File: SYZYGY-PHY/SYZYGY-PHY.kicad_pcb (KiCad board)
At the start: 4 copper layers, 57.7 x 27 mm, 45 parts, among them J1 QTH-020-01-X-D-DP-A, J2 ARJM11C7-502-KB-EW2, J3 Conn_01x10, U1 GPY111, U2 TXB0106RGY, U3 TXB0106RGY, Y1 Crystal_GND24

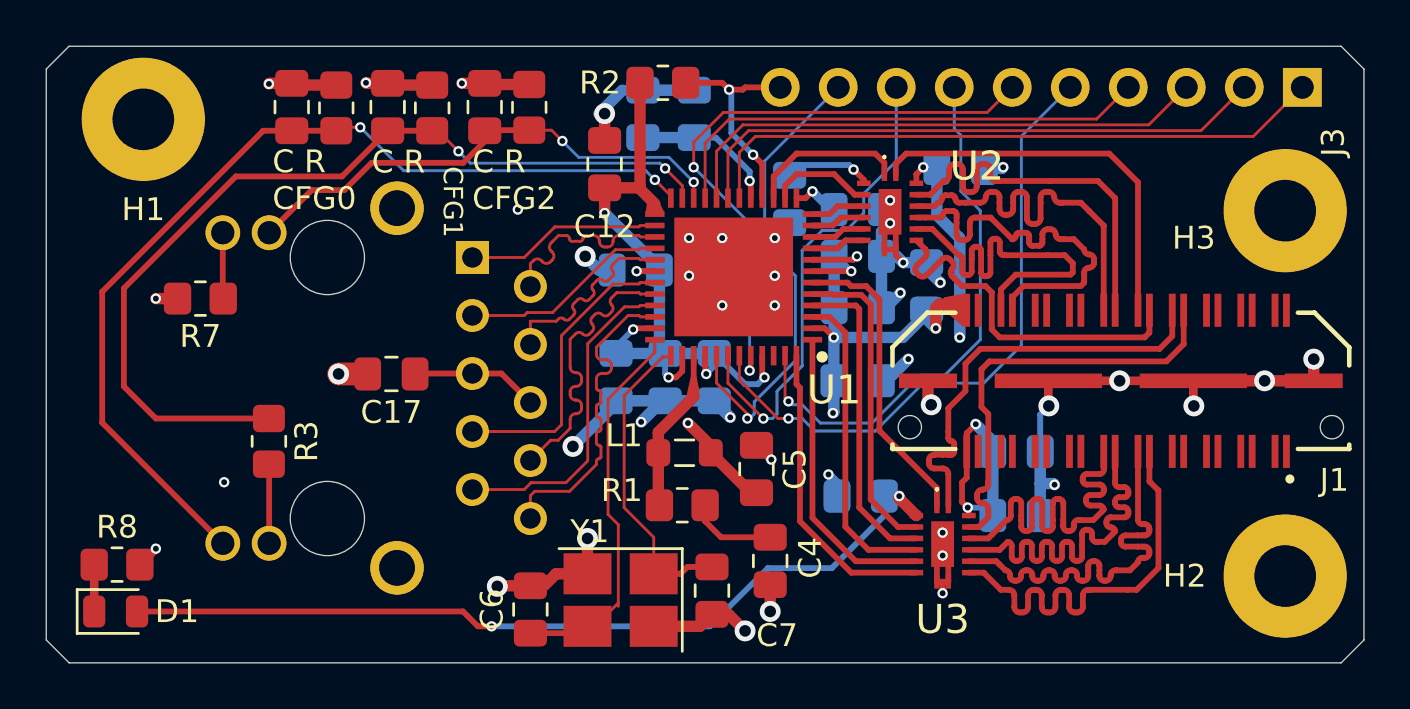
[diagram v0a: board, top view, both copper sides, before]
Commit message: misc changes + SYZYGY-PHY fixes
fix up KiCad paths to be slightly friendlier to sharing between
machines; assert that we only want to use the library from `../`
relative so the 3d model path is valid.

SYZYGY-PHY fixes:
- add startup RC circuit to hold reset low for >1ms
- add calibration resistors between PHY C+/- and GND
- remove VDDLC from 3.3V net in schematic (not fully routed in PCB)
- update clock to a more frequency stable model, change CL caps accordingly
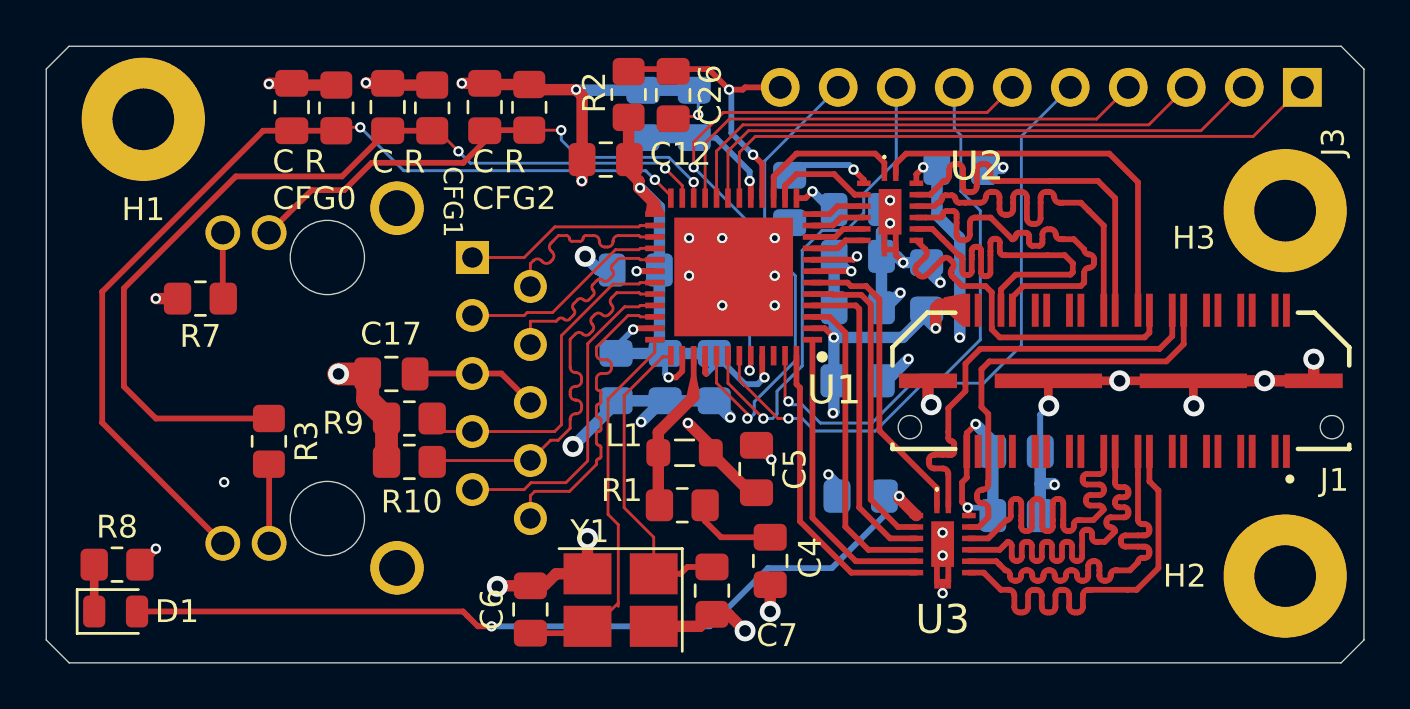
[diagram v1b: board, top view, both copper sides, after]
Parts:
- added C26: 100n, Capacitor_SMD:C_0805_2012Metric_Pad1.18x1.45mm_HandSolder, F.Cu at (117.5, 64.1)
- added R10: 16k, Resistor_SMD:R_0805_2012Metric_Pad1.20x1.40mm_HandSolder, F.Cu at (105.9, 80.2)
- added R9: 16k, Resistor_SMD:R_0805_2012Metric_Pad1.20x1.40mm_HandSolder, F.Cu at (105.9, 78.3)
- C6, C7: value 33p -> 20p
- moved R2 1.59 mm to (115.5, 64.1), turned to 90 degrees
- moved C12 0.21 mm to (114.5, 67.0), turned to 180 degrees
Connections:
- U1 pad 40: +3V3 -> /VDDLC
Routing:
- net GND: track 83.2 -> 95.3 mm, vias 43 -> 44
- net /TD3-: track 12.8 -> 17.2 mm
- net +3V3: track 109.4 -> 106.2 mm, vias 13 -> 12
- net /RSTN: track 9.66 -> 12.4 mm
- net /TD3+: track 13.0 -> 15.0 mm
- net /VDDLC: track 33.9 -> 34.8 mm

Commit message: fixed power lines, added keepout underneath RJ45, added ground stippling
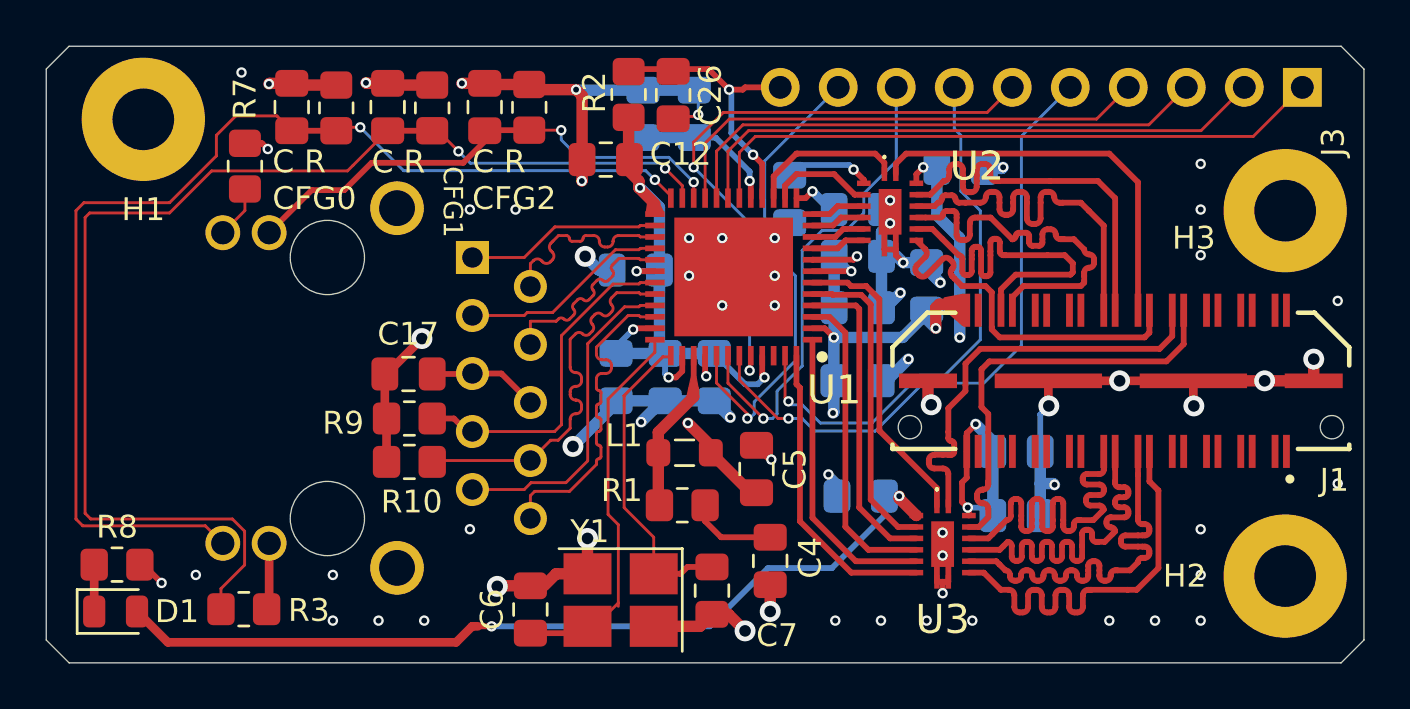
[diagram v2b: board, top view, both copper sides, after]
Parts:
- moved R3 7.43 mm to (98.7, 86.7), turned to 0 degrees
- moved R7 6.12 mm to (98.7, 67.2), turned to 90 degrees
- moved C17 0.75 mm to (105.9, 76.3)
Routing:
- net /LED1: track 40.1 -> 53.4 mm
- net /LED0: track 42.4 -> 50.3 mm
- net +3V3: track 106.2 -> 102.6 mm
- net GND: track 95.3 -> 96.4 mm, vias 44 -> 66
- net Net-(J2-CT1): track 5.58 -> 4.83 mm
- net /RIGHT_CAT: track 2.89 -> 2.32 mm
- net /LEFT_AN: track 3.47 -> 2.93 mm
- net /VDDLC: track 34.8 -> 34.9 mm, vias 4 -> 5

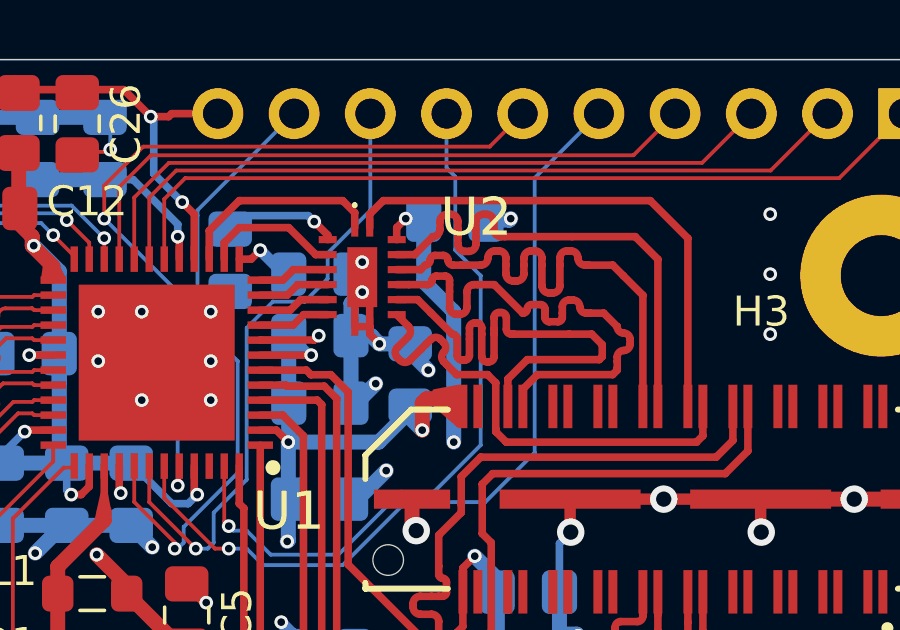
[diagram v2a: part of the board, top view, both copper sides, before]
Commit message: truly the Rx and Tx RGMII channels are length tuned very nearly exactly length tuned
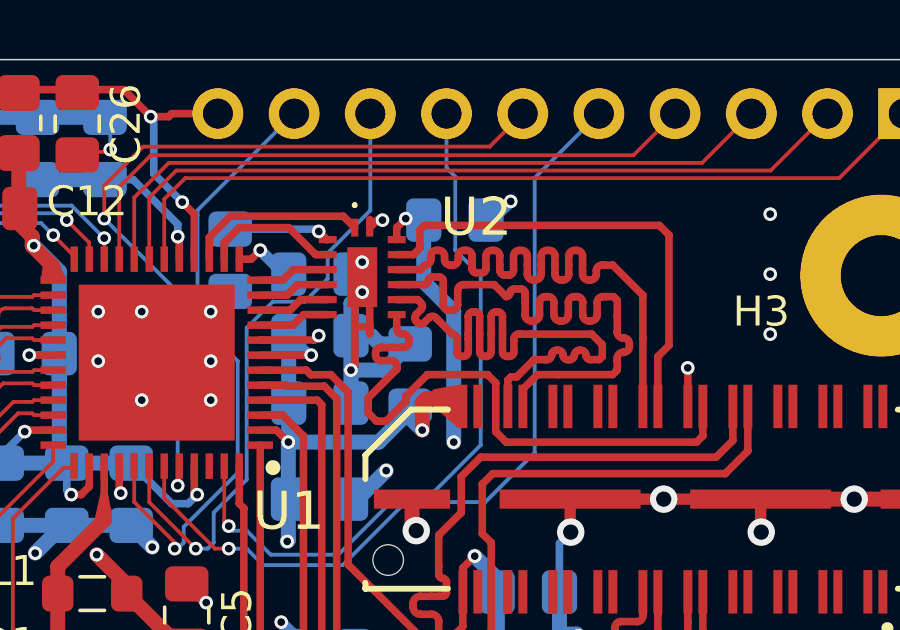
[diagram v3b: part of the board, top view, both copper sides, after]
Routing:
- net /TX_CLK_L: track 16.2 -> 20.4 mm
- net /TXD2_L: track 17.2 -> 20.3 mm
- net /TX_CTL_L: track 17.4 -> 14.3 mm, vias 0 -> 2
- net /TXD1_L: track 17.2 -> 20.2 mm
- net /TXD3_L: track 17.2 -> 20.3 mm
- net GND: track 96.4 -> 98.3 mm, vias 66 -> 64
- net /TXD0_L: track 17.2 -> 15.8 mm
- net /TX_CTL: track 6.88 -> 6.03 mm

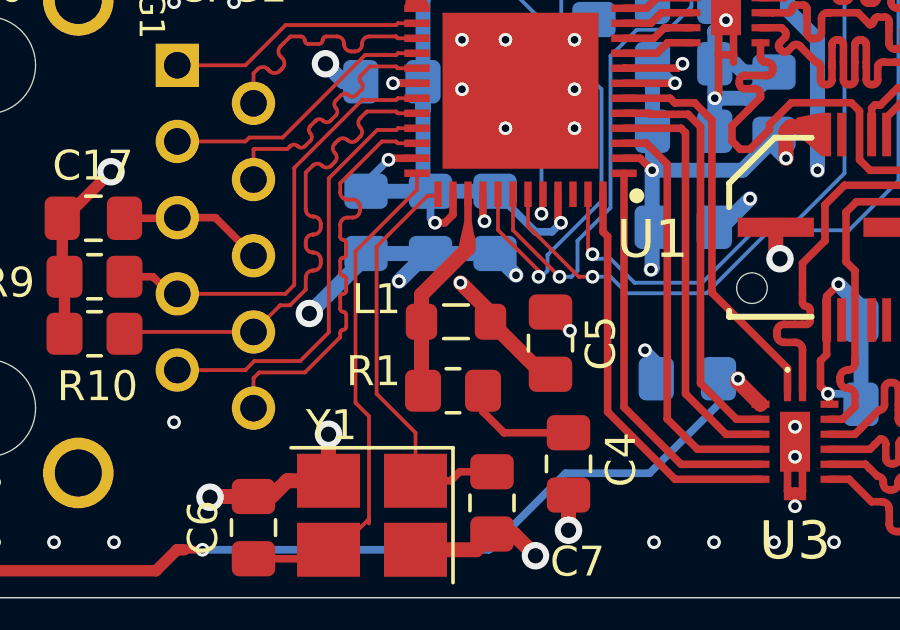
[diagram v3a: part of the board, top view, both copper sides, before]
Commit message: adding inductor footprint for 2016 metric sized inductor, and changed L1 footprint and added to the pcb, updated the schematic with the new inductor part and datasheet link
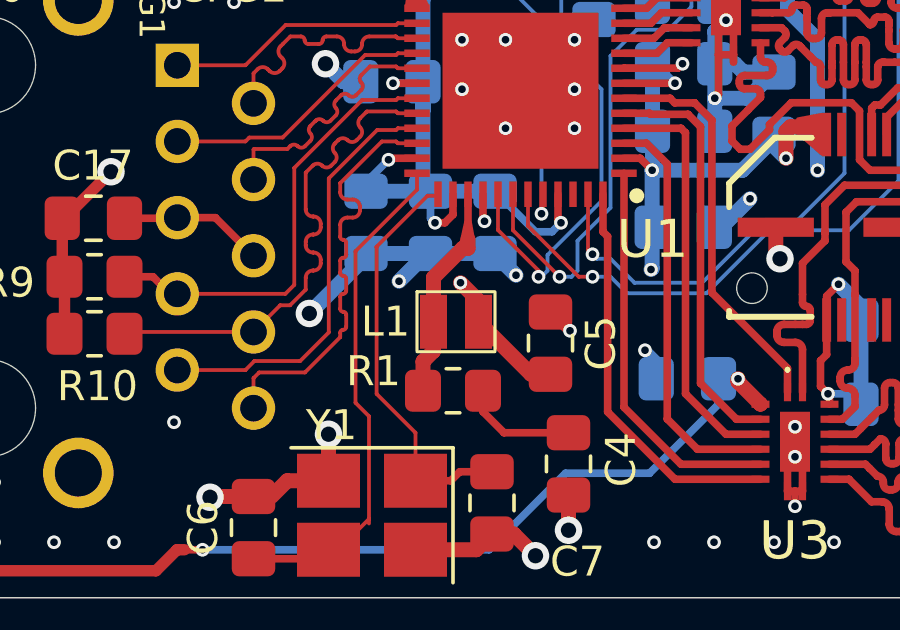
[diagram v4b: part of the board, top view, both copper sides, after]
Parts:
- L1: footprint Inductor_SMD:L_0805_2012Metric_Pad1.05x1.20mm_HandSolder -> local:Inductor 0806 (2016 metric)
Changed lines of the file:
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@@
 		)
 	)
-	(footprint "Inductor_SMD:L_0805_2012Metric_Pad1.05x1.20mm_HandSolder"
+	(footprint "local:Inductor 0806 (2016 metric)"
 		(layer "F.Cu")
 		(at 117.95 79.8)
-		(descr "Inductor SMD 0805 (2012 Metric), square (rectangular) end terminal, IPC_7351 nominal with elongated pad for handsoldering. (Body size source: IPC-SM-782 page 80, https://www.pcb-3d.com/wordpress/wp-content/uploads/ipc-sm-782a_amendment_1_and_2.pdf), generated with kicad-footprint-generator")
-		(tags "inductor handsolder")
+		(tags "Inductor")
 		(property "Reference" "L1"
-			(at -2.65 -0.75 0)
+			(at -2.35 0 0)
+			(unlocked yes)
 			(layer "F.SilkS")
 			(effects
@@
 		)
 		(property "Value" "4.7u"
-			(at 0 1.55 0)
+			(at 0 1 0)
+			(unlocked yes)
 			(layer "F.Fab")
 			(effects
@@
 			)
 		)
-		(property "Footprint" "Inductor_SMD:L_0805_2012Metric_Pad1.05x1.20mm_HandSolder"
+		(property "Footprint" "local:Inductor 0806 (2016 metric)"
 			(at 0 0 0)
 			(unlocked yes)
@@
 			(effects
 				(font
-					(size 1.27 1.27)
+					(size 1 1)
 					(thickness 0.15)
 				)
@@
 			(effects
 				(font
-					(size 1.27 1.27)
+					(size 1 1)
 					(thickness 0.15)
 				)
@@
 			(effects
 				(font
-					(size 1.27 1.27)
+					(size 1 1)
 					(thickness 0.15)
 				)
@@
 		(sheetfile "SYZYGY-PHY.kicad_sch")
 		(attr smd)
-		(fp_line
-			(start -0.410242 -0.56)
-			(end 0.410242 -0.56)
+		(fp_rect
+			(start -1.3 -1)
+			(end 1.3 1)
 			(stroke
-				(width 0.12)
-				(type solid)
-			)
-			(layer "F.SilkS")
-		)
-		(fp_line
-			(start -0.410242 0.56)
-			(end 0.410242 0.56)
-			(stroke
-				(width 0.12)
-				(type solid)
+				(width 0.1)
+				(type default)
 			)
+			(fill none)
 			(layer "F.SilkS")
 		)
-		(fp_line
-			(start -1.92 -0.85)
-			(end 1.92 -0.85)
-			(stroke
-				(width 0.05)
-				(type solid)
-			)
-			(layer "F.CrtYd")
-		)
-		(fp_line
-			(start -1.92 0.85)
-			(end -1.92 -0.85)
-			(stroke
-				(width 0.05)
-				(type solid)
-			)
-			(layer "F.CrtYd")
-		)
-		(fp_line
-			(start 1.92 -0.85)
-			(end 1.92 0.85)
-			(stroke
-				(width 0.05)
-				(type solid)
-			)
-			(layer "F.CrtYd")
-		)
-		(fp_line
-			(start 1.92 0.85)
-			(end -1.92 0.85)
+		(fp_rect
+			(start -1.4 -1.1)
+			(end 1.4 1.1)
 			(stroke
 				(width 0.05)
-				(type solid)
+				(type default)
 			)
+			(fill none)
 			(layer "F.CrtYd")
 		)
-		(fp_line
-			(start -1 -0.45)
-			(end 1 -0.45)
-			(stroke
-				(width 0.1)
-				(type solid)
-			)
-			(layer "F.Fab")
-		)
-		(fp_line
-			(start -1 0.45)
-			(end -1 -0.45)
-			(stroke
-				(width 0.1)
-				(type solid)
-			)
-			(layer "F.Fab")
-		)
-		(fp_line
-			(start 1 -0.45)
-			(end 1 0.45)
-			(stroke
-				(width 0.1)
-				(type solid)
-			)
-			(layer "F.Fab")
-		)
-		(fp_line
-			(start 1 0.45)
-			(end -1 0.45)
-			(stroke
-				(width 0.1)
-				(type solid)
-			)
-			(layer "F.Fab")
-		)
 		(fp_text user "${REFERENCE}"
-			(at 0 0 0)
+			(at 0 2.5 0)
+			(unlocked yes)
 			(layer "F.Fab")
 			(effects
 				(font
-					(size 0.5 0.5)
-					(thickness 0.08)
+					(size 1 1)
+					(thickness 0.15)
 				)
 			)
 		)
-		(pad "1" smd roundrect
-			(at -1.15 0)
-			(size 1.05 1.2)
+		(pad "1" smd rect
+			(at -0.75 0)
+			(size 0.9 1.8)
 			(layers "F.Cu" "F.Paste" "F.Mask")
-			(roundrect_rratio 0.238095)
 			(net 54 "/REG0")
 			(pinfunction "1")
 			(pintype "passive")
 		)
-		(pad "2" smd roundrect
-			(at 1.15 0)
-			(size 1.05 1.2)
+		(pad "2" smd rect
+			(at 0.75 0)
+			(size 0.9 1.8)
 			(layers "F.Cu" "F.Paste" "F.Mask")
-			(roundrect_rratio 0.238095)
 			(net 51 "/VDDLC")
 			(pinfunction "2")
 			(pintype "passive")
 		)
-		(model "${KICAD8_3DMODEL_DIR}/Inductor_SMD.3dshapes/L_0805_2012Metric.wrl"
-			(offset
-				(xyz 0 0 0)
-			)
-			(scale
-				(xyz 1 1 1)
-			)
-			(rotate
-				(xyz 0 0 0)
-			)
-		)
 	)
 	(footprint "LED_SMD:LED_0805_2012Metric"
@@
 	)
 	(segment
-		(start 120.85 81.55)
-		(end 121.1 81.55)
-		(width 0.5)
-		(layer "F.Cu")
-		(net 51)
-	)
-	(segment
 		(start 122.85 68.65)
 		(end 123.25 68.65)
@@
 	)
 	(segment
-		(start 119.1 79.5)
+		(start 118.7 79.1)
 		(end 118.1 78.5)
 		(width 0.5)
@@
 	)
 	(segment
-		(start 119.1 79.8)
-		(end 120.85 81.55)
-		(width 0.5)
-		(layer "F.Cu")
-		(net 51)
-	)
-	(segment
 		(start 118.85 76.4)
 		(end 118.9 76.45)
@@
 	)
 	(segment
-		(start 123.25 68.65)
-		(end 123.55 68.35)
-		(width 0.254)
+		(start 118.7 79.8)
+		(end 118.7 79.1)
+		(width 0.5)
 		(layer "F.Cu")
 		(net 51)
 	)
 	(segment
-		(start 119.1 79.8)
-		(end 119.1 79.5)
-		(width 0.5)
+		(start 123.25 68.65)
+		(end 123.55 68.35)
+		(width 0.254)
 		(layer "F.Cu")
 		(net 51)
@@
 	)
 	(segment
+		(start 120.45 81.55)
+		(end 118.7 79.8)
+		(width 0.5)
+		(layer "F.Cu")
+		(net 51)
+	)
+	(segment
 		(start 120.85 67.95)
 		(end 120.8 67.9)
@@
 		(net 51)
 	)
+	(segment
+		(start 121.1 81.55)
+		(end 120.45 81.55)
+		(width 0.5)
+		(layer "F.Cu")
+		(net 51)
+	)
 	(via
 		(at 123.55 68.35)
@@
 	)
 	(segment
-		(start 116.8 79.8)
-		(end 116.8 78.9)
+		(start 117.2 78.325)
+		(end 117.2 79.8)
 		(width 0.5)
 		(layer "F.Cu")
@@
 	)
 	(segment
-		(start 116.8 79.8)
-		(end 116.8 82.05)
+		(start 118.35 77.35)
+		(end 118.175 77.35)
 		(width 0.5)
 		(layer "F.Cu")
@@
 	)
 	(segment
-		(start 116.8 78.9)
-		(end 118.35 77.35)
+		(start 116.85 81.125)
+		(end 116.85 82.1)
 		(width 0.5)
 		(layer "F.Cu")
@@
 	)
 	(segment
-		(start 118.35 77.35)
-		(end 118.35 77.05)
+		(start 118.175 77.35)
+		(end 117.2 78.325)
+		(width 0.5)
+		(layer "F.Cu")
+		(net 54)
+	)
+	(segment
+		(start 118.35 77.05)
+		(end 118.35 77.35)
 		(width 0.5)
 		(layer "F.Cu")
@@
 		(width 0.5)
 		(layer "F.Cu")
+		(net 54)
+	)
+	(segment
+		(start 117.2 79.8)
+		(end 117.2 80.775)
+		(width 0.5)
+		(layer "F.Cu")
+		(net 54)
+	)
+	(segment
+		(start 117.2 80.775)
+		(end 116.85 81.125)
+		(width 0.5)
+		(layer "F.Cu")

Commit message: do we like more text? Cant stop wont stop editing the board
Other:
- board text added: "1Gbps PHY over SYZYGY for BeagleV-fire"
- board text added: "@rustbox rev 1 08-17-2024"
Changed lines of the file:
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@@
 		(tags "resistor handsolder")
 		(property "Reference" "R8"
-			(at 0 -1.65 0)
+			(at 2.65 0.05 0)
 			(layer "F.SilkS")
 			(effects
@@
 		(tags "mounting hole 2.7mm m2.5")
 		(property "Reference" "H1"
-			(at 0 3.95 0)
-			(layer "F.SilkS")
+			(at 3.85 -1.05 -0)
+			(layer "B.SilkS")
 			(effects
 				(font
@@
 					(thickness 0.15)
 				)
+				(justify mirror)
 			)
 		)
@@
 		)
 	)
+	(gr_text "   1Gbps PHY\n   over SYZYGY\nfor BeagleV-fire\n"
+		(at 95.25 68.85 270)
+		(layer "F.SilkS")
+		(effects
+			(font
+				(size 1 1)
+				(thickness 0.15)
+			)
+			(justify left bottom)
+		)
+	)
 	(gr_text "C R"
 		(at 104.25 67.65 0)
 		(layer "F.SilkS")
 		(effects
+			(font
+				(size 1 1)
+				(thickness 0.15)
+			)
+			(justify left bottom)
+		)
+	)
+	(gr_text "@rustbox\nrev 1 08-17-2024"
+		(at 91.825 68.85 -90)
+		(layer "F.SilkS")
+		(effects
